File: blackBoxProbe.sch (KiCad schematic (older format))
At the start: 81 parts, among them J1 USB-ID, J2 JTAG_2X05, J3 JTAG_2X05, J4 Conn_01x04, Q1 Q_NMOS_DUAL, U1 MCP1702-MB, U2 USBLC6-2, U3 STM32F103CBT, U4 74X2T45, U5 74X2T45, U6 74X2T45, U7 74X2T45, Y1 Crystal

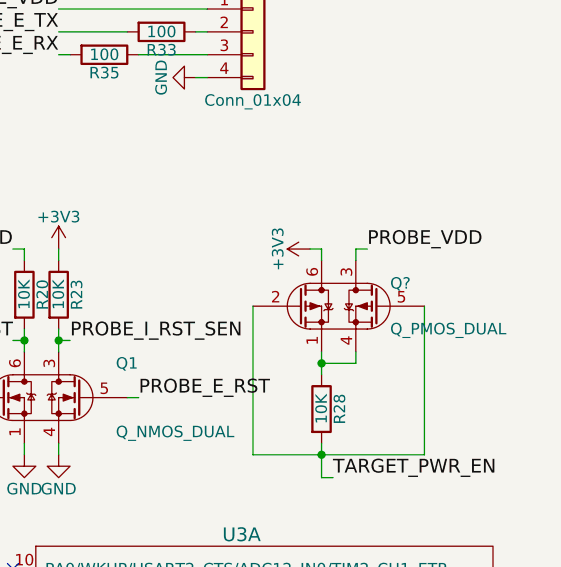
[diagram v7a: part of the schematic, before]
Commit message: DONE: imported netlist to PCB WIP: initial placing, thinking about replacing all R and C by 0402
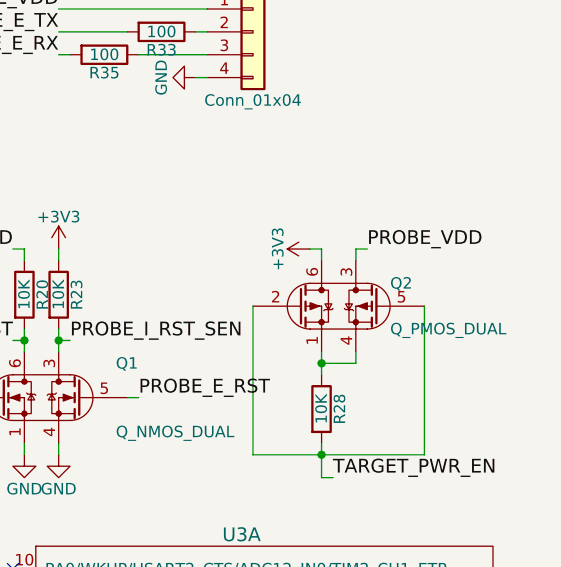
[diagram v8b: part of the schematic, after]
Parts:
- J4: footprint (none) -> Pin_Headers:Pin_Header_Angled_1x04_Pitch2.54mm
- S1, S2: footprint SquantorButtons:SquantorButtons-DTSM3 -> SquantorButtons:DTSM3
- U2: footprint (none) -> TO_SOT_Packages_SMD:SOT-23-6_Handsoldering
- U3: footprint (none) -> SquantorIC:SOT313-2
- gave numbers to parts that had none: 1
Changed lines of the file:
@@
 F 0 "U2" H 2500 3350 60  0000 C CNN
 F 1 "USBLC6-2" H 2500 2850 60  0000 C CNN
-F 2 "" H 2350 3050 60  0001 C CNN
+F 2 "TO_SOT_Packages_SMD:SOT-23-6_Handsoldering" H 2350 3050 60  0001 C CNN
 F 3 "" H 2350 3050 60  0001 C CNN
 	1    2500 3100
@@
 F 0 "U3" H 10000 6450 60  0000 C CNN
 F 1 "STM32F103CBT" H 10000 4250 60  0000 C CNN
-F 2 "" H 9000 5450 60  0001 C CNN
+F 2 "SquantorIC:SOT313-2" H 9000 5450 60  0001 C CNN
 F 3 "" H 9000 5450 60  0001 C CNN
 	1    10000 5350
@@
 F 0 "U3" H 7050 6450 60  0000 C CNN
 F 1 "STM32F103CBT" H 7050 4250 60  0000 C CNN
-F 2 "" H 6050 5450 60  0001 C CNN
+F 2 "SquantorIC:SOT313-2" H 6050 5450 60  0001 C CNN
 F 3 "" H 6050 5450 60  0001 C CNN
 	2    7050 5350
@@
 F 0 "U3" H 4350 6450 60  0000 C CNN
 F 1 "STM32F103CBT" H 4350 4250 60  0000 C CNN
-F 2 "" H 3350 5450 60  0001 C CNN
+F 2 "SquantorIC:SOT313-2" H 3350 5450 60  0001 C CNN
 F 3 "" H 3350 5450 60  0001 C CNN
 	3    4350 5350
@@
 F 0 "S2" H 3600 6450 60  0000 C CNN
 F 1 "2pin_tact_switch" H 3600 6100 60  0000 C CNN
-F 2 "SquantorButtons:SquantorButtons-DTSM3" H 3600 6200 60  0001 C CNN
+F 2 "SquantorButtons:DTSM3" H 3600 6200 60  0001 C CNN
 F 3 "" H 3600 6200 60  0001 C CNN
 	1    3600 6200
@@
 F 0 "S1" H 800 5150 60  0000 C CNN
 F 1 "2pin_tact_switch" H 800 4800 60  0000 C CNN
-F 2 "SquantorButtons:SquantorButtons-DTSM3" H 800 4900 60  0001 C CNN
+F 2 "SquantorButtons:DTSM3" H 800 4900 60  0001 C CNN
 F 3 "" H 800 4900 60  0001 C CNN
 	1    800  4900
@@
 F 0 "J4" H 10050 2250 50  0000 C CNN
 F 1 "Conn_01x04" H 10050 1750 50  0000 C CNN
-F 2 "" H 10050 2050 50  0001 C CNN
+F 2 "Pin_Headers:Pin_Header_Angled_1x04_Pitch2.54mm" H 10050 2050 50  0001 C CNN
 F 3 "" H 10050 2050 50  0001 C CNN
 	1    10050 2050
@@
 Connection ~ 10550 800
 $Comp
-L Q_PMOS_DUAL Q?
+L Q_PMOS_DUAL Q2
 U 1 1 5B2C36DB
 P 10400 3250
-F 0 "Q?" H 10650 3350 50  0000 L CNN
+F 0 "Q2" H 10650 3350 50  0000 L CNN
 F 1 "Q_PMOS_DUAL" H 10650 3150 50  0000 L CNN
 F 2 "TO_SOT_Packages_SMD:SOT-363_SC-70-6_Handsoldering" H 10450 3350 50  0001 C CNN
